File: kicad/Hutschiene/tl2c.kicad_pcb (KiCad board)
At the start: 4 copper layers, 175.9 x 86.5 mm, 76 parts, among them IC101 ATTINY20-X, P101 12VDC, P102 RJ45, P103 CTL CONN, P104 TPI Header, P105 DRV CONN, P106 240VAC, P108 UG, P109 5VDC, P110 EG, P111 OG, P201 Mode_Bridge, P501 CONN_PIR_OG, P502 CONN_PIR_EG, P503 CONN_PIR_UG, Q301 IRLML2502, Q302 IRLML2502, Q303 IRLML2502, Q401 IRLML2502, Q402 IRLML2502, Q403 IRLML2502, SW101 TL3315NF160Q, U201 LF120ABDT-TR, U202 TPS70933

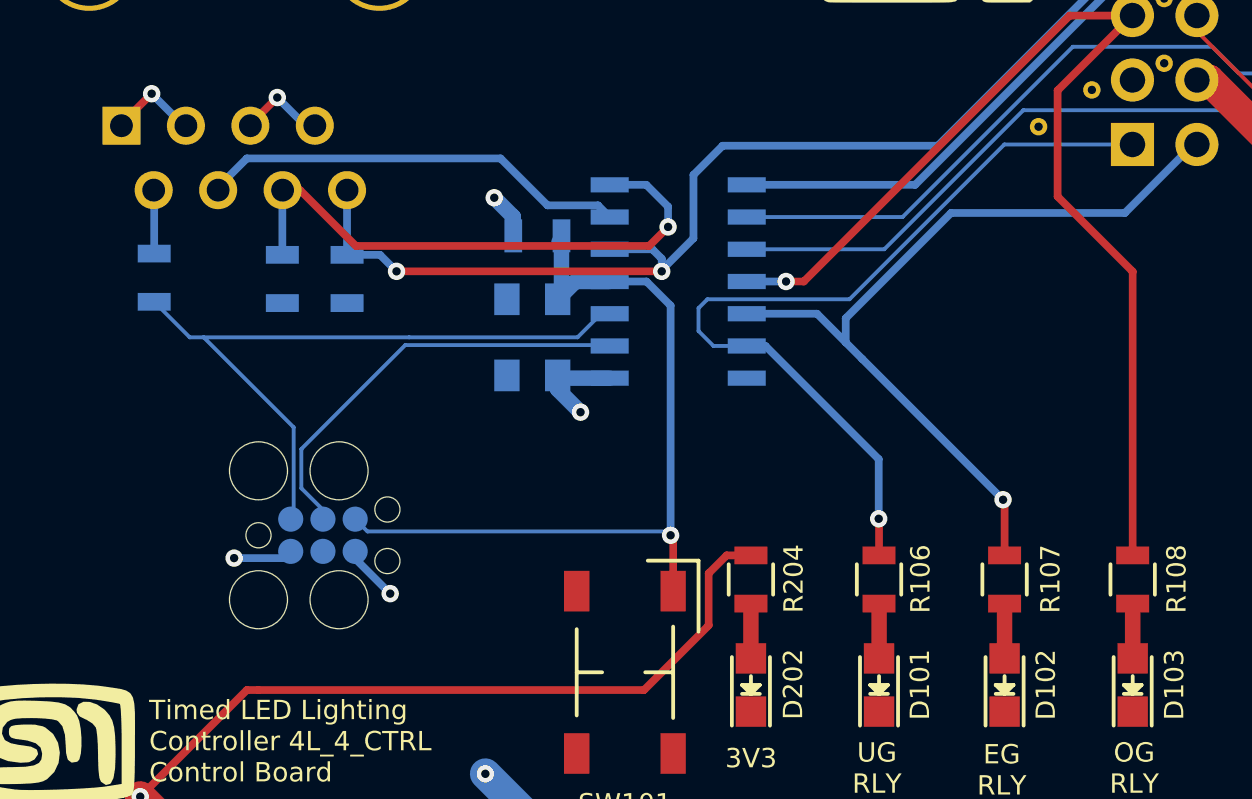
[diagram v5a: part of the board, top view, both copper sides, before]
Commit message: Flipped the programming header properly
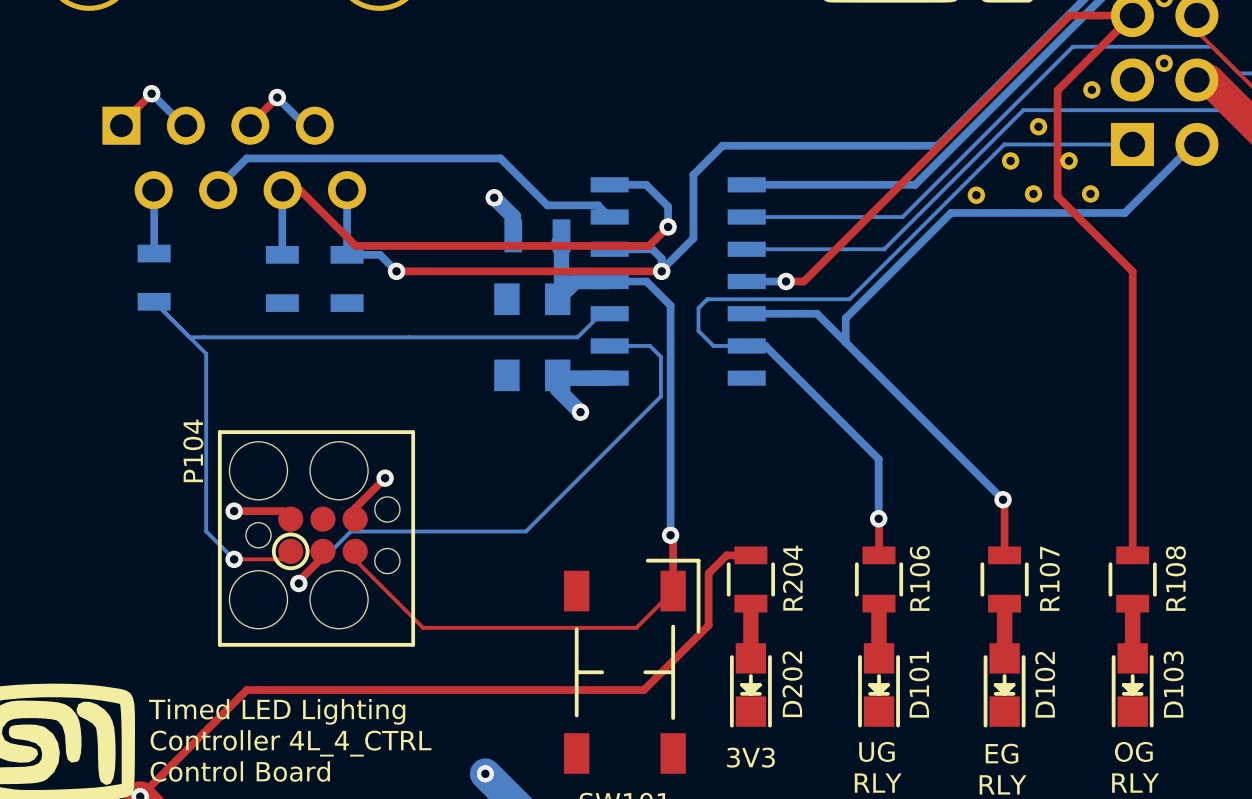
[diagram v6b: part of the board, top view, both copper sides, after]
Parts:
- added REF**31: Stitch_VIA, tl2c-footprint:Stitch_VIA, F.Cu at (205.1, 99.8)
- added REF**31: Stitch_VIA, tl2c-footprint:Stitch_VIA, F.Cu at (202.8, 99.8)
- added REF**31: Stitch_VIA, tl2c-footprint:Stitch_VIA, F.Cu at (204.2, 98.5)
- added REF**31: Stitch_VIA, tl2c-footprint:Stitch_VIA, F.Cu at (201.9, 98.5)
- added REF**31: Stitch_VIA, tl2c-footprint:Stitch_VIA, F.Cu at (200.6, 99.8)
- P104: moved to F.Cu
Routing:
- net /TPICLK: track 17.0 -> 22.8 mm, vias 0 -> 1
- net /TPIDATA: track 27.6 -> 32.7 mm, vias 0 -> 1
- net /~Reset: track 32.3 -> 34.2 mm

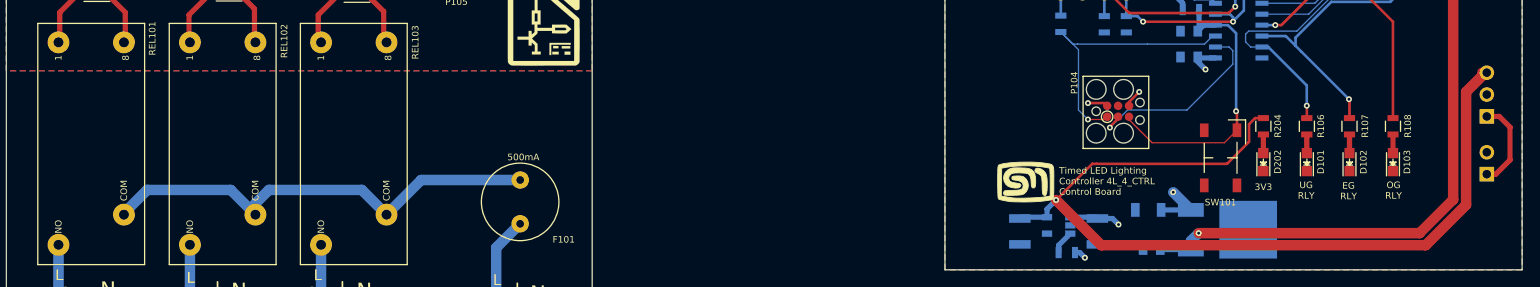
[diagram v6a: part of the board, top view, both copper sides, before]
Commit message: Fixed some labels and text
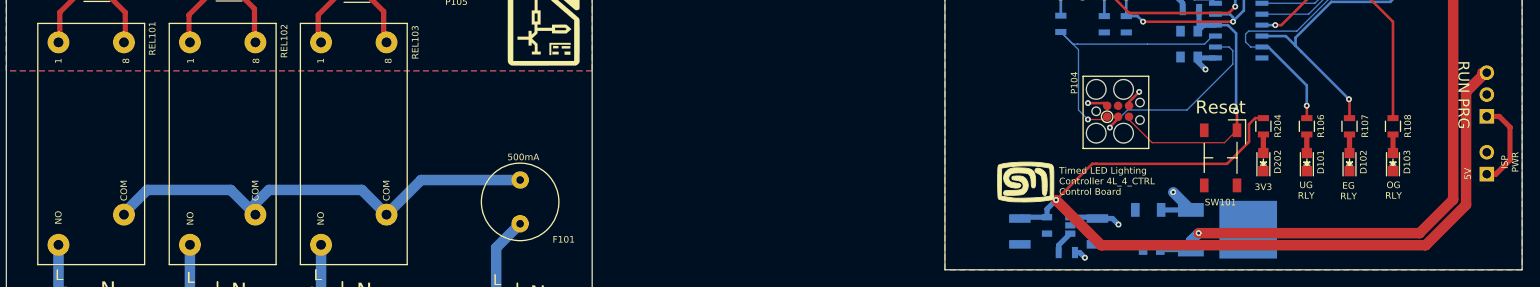
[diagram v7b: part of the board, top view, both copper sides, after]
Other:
- board text added: "Reset"
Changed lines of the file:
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@@
     (area 20.250001 40.4 248.26 176.820001)
     (thickness 1.6)
-    (drawings 100)
+    (drawings 104)
     (tracks 365)
     (zones 0)
@@
       (effects (font (size 0.762 0.762) (thickness 0.127)))
     )
-    (fp_text user 8 (at 10 4 90) (layer F.SilkS)
+    (fp_text user 8 (at 9.65 4.05 90) (layer F.SilkS)
       (effects (font (size 0.762 0.762) (thickness 0.127)))
     )
-    (fp_text user 1 (at 10 -3.8 90) (layer F.SilkS)
+    (fp_text user 1 (at 9.65 -3.8 90) (layer F.SilkS)
       (effects (font (size 0.762 0.762) (thickness 0.127)))
     )
@@
       (effects (font (size 0.762 0.762) (thickness 0.127)))
     )
-    (fp_text user NO (at -9.6 -3.8 90) (layer F.SilkS)
+    (fp_text user NO (at -8.55 -3.8 90) (layer F.SilkS)
       (effects (font (size 0.762 0.762) (thickness 0.127)))
     )
-    (fp_text user NO (at -9.6 -3.8 90) (layer B.SilkS)
+    (fp_text user NO (at -8.6 -3.75 90) (layer B.SilkS)
       (effects (font (size 0.762 0.762) (thickness 0.127)) (justify mirror))
     )
@@
       (effects (font (size 0.762 0.762) (thickness 0.127)) (justify mirror))
     )
-    (fp_text user 8 (at 10 4 90) (layer B.SilkS)
+    (fp_text user 8 (at 9.65 4.05 90) (layer B.SilkS)
       (effects (font (size 0.762 0.762) (thickness 0.127)) (justify mirror))
     )
-    (fp_text user 1 (at 10 -3.8 90) (layer B.SilkS)
+    (fp_text user 1 (at 9.6 -3.85 90) (layer B.SilkS)
       (effects (font (size 0.762 0.762) (thickness 0.127)) (justify mirror))
     )
@@
       (effects (font (size 0.762 0.762) (thickness 0.127)))
     )
-    (fp_text user 8 (at 10 4 90) (layer F.SilkS)
+    (fp_text user 8 (at 9.65 3.89 90) (layer F.SilkS)
       (effects (font (size 0.762 0.762) (thickness 0.127)))
     )
-    (fp_text user 1 (at 10 -3.8 90) (layer F.SilkS)
+    (fp_text user 1 (at 9.65 -3.71 90) (layer F.SilkS)
       (effects (font (size 0.762 0.762) (thickness 0.127)))
     )
@@
       (effects (font (size 0.762 0.762) (thickness 0.127)))
     )
-    (fp_text user NO (at -9.6 -3.8 90) (layer F.SilkS)
+    (fp_text user NO (at -8.65 -3.76 90) (layer F.SilkS)
       (effects (font (size 0.762 0.762) (thickness 0.127)))
     )
-    (fp_text user NO (at -9.6 -3.8 90) (layer B.SilkS)
+    (fp_text user NO (at -8.75 -3.71 90) (layer B.SilkS)
       (effects (font (size 0.762 0.762) (thickness 0.127)) (justify mirror))
     )
@@
       (effects (font (size 0.762 0.762) (thickness 0.127)) (justify mirror))
     )
-    (fp_text user 8 (at 10 4 90) (layer B.SilkS)
+    (fp_text user 8 (at 9.7 3.89 90) (layer B.SilkS)
       (effects (font (size 0.762 0.762) (thickness 0.127)) (justify mirror))
     )
-    (fp_text user 1 (at 10 -3.8 90) (layer B.SilkS)
+    (fp_text user 1 (at 9.6 -3.71 90) (layer B.SilkS)
       (effects (font (size 0.762 0.762) (thickness 0.127)) (justify mirror))
     )
@@
       (effects (font (size 0.762 0.762) (thickness 0.127)))
     )
-    (fp_text user 8 (at 10 4 90) (layer F.SilkS)
+    (fp_text user 8 (at 9.65 4.02 90) (layer F.SilkS)
       (effects (font (size 0.762 0.762) (thickness 0.127)))
     )
-    (fp_text user 1 (at 10 -3.8 90) (layer F.SilkS)
+    (fp_text user 1 (at 9.65 -3.83 90) (layer F.SilkS)
       (effects (font (size 0.762 0.762) (thickness 0.127)))
     )
@@
       (effects (font (size 0.762 0.762) (thickness 0.127)))
     )
-    (fp_text user NO (at -9.6 -3.8 90) (layer F.SilkS)
+    (fp_text user NO (at -8.65 -3.83 90) (layer F.SilkS)
       (effects (font (size 0.762 0.762) (thickness 0.127)))
     )
-    (fp_text user NO (at -9.6 -3.8 90) (layer B.SilkS)
+    (fp_text user NO (at -8.6 -3.83 90) (layer B.SilkS)
       (effects (font (size 0.762 0.762) (thickness 0.127)) (justify mirror))
     )
@@
       (effects (font (size 0.762 0.762) (thickness 0.127)) (justify mirror))
     )
-    (fp_text user 8 (at 10 4 90) (layer B.SilkS)
+    (fp_text user 8 (at 9.65 4.02 90) (layer B.SilkS)
       (effects (font (size 0.762 0.762) (thickness 0.127)) (justify mirror))
     )
-    (fp_text user 1 (at 10 -3.8 90) (layer B.SilkS)
+    (fp_text user 1 (at 9.6 -3.83 90) (layer B.SilkS)
       (effects (font (size 0.762 0.762) (thickness 0.127)) (justify mirror))
     )
@@
       (net 39 /Neutral))
   )
+  (gr_text 5V (at 215.4 120.45 90) (layer F.SilkS)
+    (effects (font (size 0.762 0.762) (thickness 0.127)))
+  )
+  (gr_text "ISP \nPWR" (at 220.3 119.1 90) (layer F.SilkS)
+    (effects (font (size 0.762 0.762) (thickness 0.127)))
+  )
+  (gr_text "RUN PRG" (at 214.9 111.3 270) (layer F.SilkS)
+    (effects (font (size 1.27 1.27) (thickness 0.127)))
+  )
+  (gr_text Reset (at 186.7 112.75) (layer F.SilkS)
+    (effects (font (size 1.5 1.5) (thickness 0.3)))
+  )
   (dimension 5 (width 0.3) (layer Eco1.User)

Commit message: Correction to the board connected and seperated out the pwr
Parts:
- removed the G*** at (160.0, 77.8)
- removed the G*** at (208.0, 122.4)
- added P107: CTL PWR, Pin_Headers:Pin_Header_Straight_1x02_Pitch2.54mm, B.Cu at (208.8, 79.9)
- added P112: DRV PWR, Pin_Headers:Pin_Header_Straight_1x02_Pitch2.54mm, F.Cu at (105.9, 76.0)
- added REF**31: Stitch_VIA, tl2c-footprint:Stitch_VIA, F.Cu at (195.8, 102.5)
- added REF**31: Stitch_VIA, tl2c-footprint:Stitch_VIA, F.Cu at (196.7, 101.3)
- added REF**31: Stitch_VIA, tl2c-footprint:Stitch_VIA, F.Cu at (194.3, 101.3)
- added REF**31: Stitch_VIA, tl2c-footprint:Stitch_VIA, F.Cu at (195.4, 100.0)
- added REF**31: Stitch_VIA, tl2c-footprint:Stitch_VIA, F.Cu at (193.4, 100.0)
- added REF**31: Stitch_VIA, tl2c-footprint:Stitch_VIA, F.Cu at (194.5, 98.6)
- added REF**31: Stitch_VIA, tl2c-footprint:Stitch_VIA, F.Cu at (196.9, 98.6)
- C204: footprint Capacitors_SMD:C_1210 -> Capacitors_SMD:C_1206
- P104: footprint tl2c-footprint:TC2030-IDC-FP_ISP_Connector -> Connect:Tag-Connect_TC2030-IDC-NL
- P105, P109, P201: moved to F.Cu
- SW101: footprint tl2c-footprint:PTS525SM15SMTR2LFS -> tl2c-footprint:TACTILE_FSM2JSMAA
- moved P109 60.0 mm to (159.4, 105.6), turned to 180 degrees
- moved P201 58.3 mm to (159.4, 109.7)
- moved C201 56.9 mm to (202.5, 77.6), turned to 0 degrees
- moved C203 49.1 mm to (202.9, 82.2), turned to 0 degrees
- moved U201 47.1 mm to (191.3, 79.9), turned to 0 degrees
- moved R202 46.0 mm to (194.7, 91.5)
- moved C202 46.0 mm to (198.2, 89.1)
- moved C204 46.0 mm to (189.2, 89.1)
- moved U202 46.0 mm to (193.7, 88.4)
- moved G*** 43.5 mm to (159.2, 78.1)
- moved G*** 41.7 mm to (216.3, 125.8), turned to 0 degrees
- moved TP101 35.4 mm to (193.4, 95.2)
- moved P104 20.9 mm to (184.4, 94.7), turned to 90 degrees
- moved SW101 3.33 mm to (183.7, 117.2), turned to 90 degrees
- moved P105 2.55 mm to (100.8, 97.8), turned to 180 degrees
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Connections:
- P103 pad 4: /Power System/U+In -> (no net)
- P105 pad 4: /DRV_PWR_IN -> (no net)
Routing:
- net /Power System/U+In: track 67.8 -> 15.7 mm, vias 1 -> 0
- net /DRV_PWR_IN: track 34.4 -> 10.4 mm
- net /Power System/5V: track 10.4 -> 4.05 mm
- net /~Reset: track 34.2 -> 40.1 mm, vias 1 -> 2
- net Net-(C204-Pad1): track 103.7 -> 98.5 mm, vias 1 -> 0
- net /RelayOG: track 44.0 -> 39.0 mm
- net /LED Driver/Relay_EG: track 12.3 -> 7.23 mm
- net /LED Driver/Relay_OG: track 8.25 -> 12.5 mm
- net /TPICLK: track 22.8 -> 19.4 mm
- net /LED Driver/Relay_UG: track 9.20 -> 12.0 mm
- net GND: track 9.35 -> 7.25 mm, vias 3 -> 2
- net /PIR_Connector/PIR_EG: track 49.7 -> 47.8 mm
- net /PIR_Connector/PIR_UG: track 38.5 -> 40.0 mm
- net /TPIDATA: track 32.7 -> 34.0 mm
- net /RelayEG: track 33.4 -> 32.1 mm
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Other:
- board text added: "+"
- board text added: "12VDC"
- board text added: "PRG"
